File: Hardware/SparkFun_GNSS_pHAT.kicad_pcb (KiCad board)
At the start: 4 copper layers, 65 x 56.8 mm, 116 parts, among them J1 Raspberry_Pi_2x20_SMD_Passthr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, J2 Conn_02x10, J3 U.FL, J4 Conn_02x10, J5 microSD_Friction, J6 USB_C_Receptacle, J7 SMA_Edge, J8 Qwiic_Vertical, U1 CAT24C512WI-GT3, U2 AP7361C-3.3V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

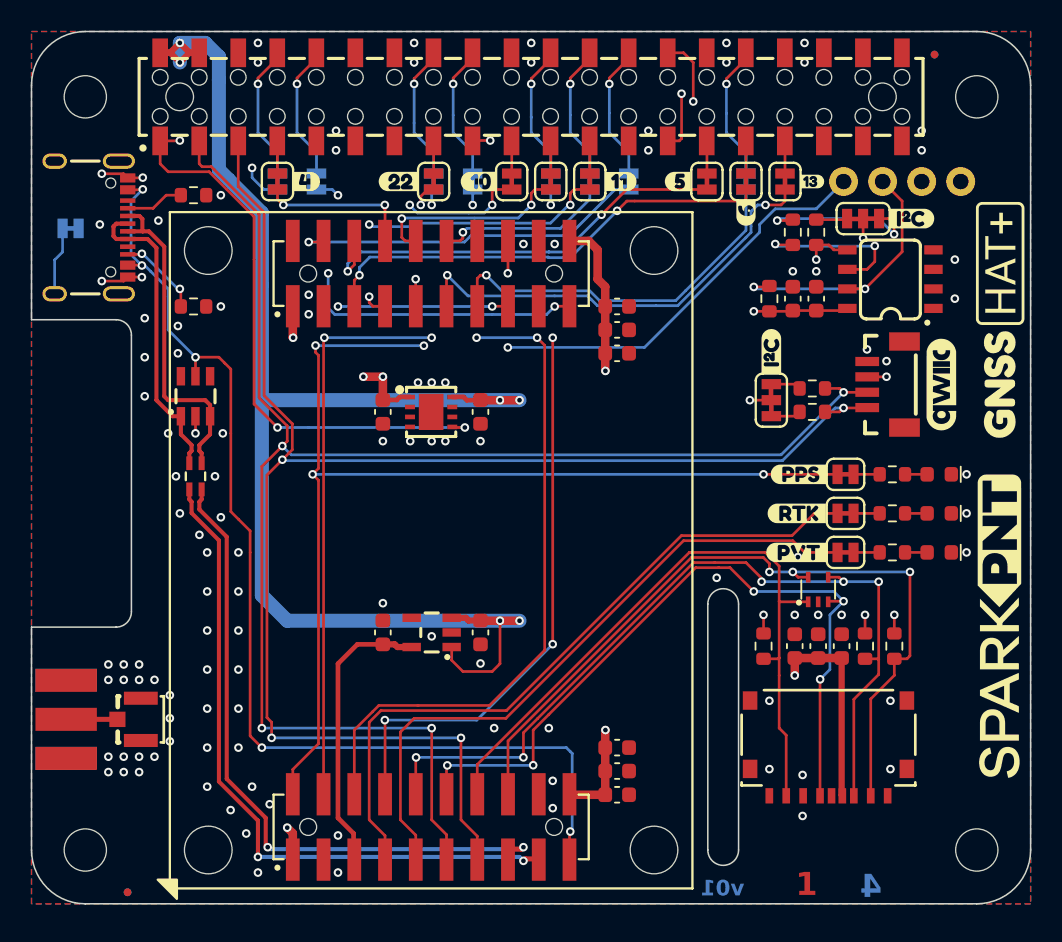
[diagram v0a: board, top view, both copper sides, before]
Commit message: pHAT routed and panelized
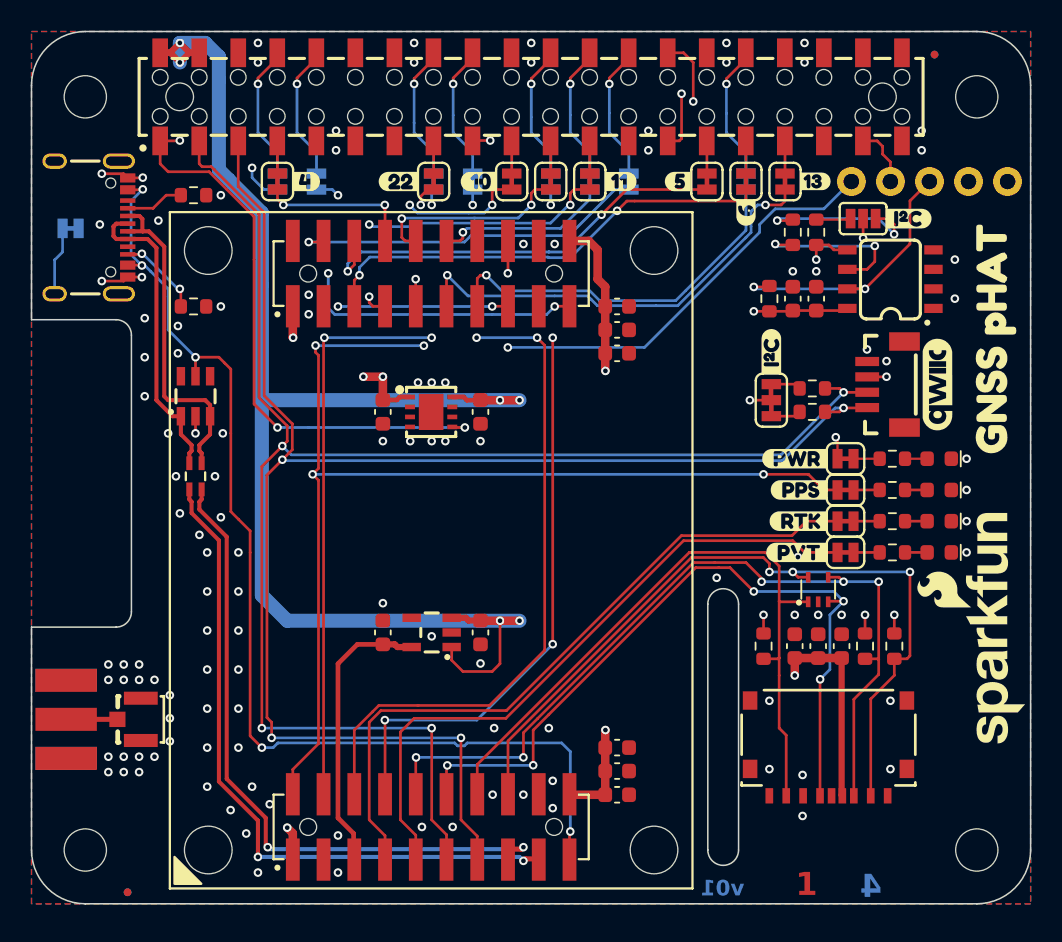
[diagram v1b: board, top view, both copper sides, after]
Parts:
- removed 3V3.1, GND.1, RST.1, WP.1: PTH, SparkFun-Connector:1x01
- removed the G*** at (178.6, 106.3)
- removed the G*** at (148.1, 97.0)
- removed REF** (x2): RPi_HAT+_8mm, SparkFun-Aesthetic:RPi_HAT+_8mm
- removed kibuzzard-678F852F (x2): G***, kibuzzard-678F852F
- removed kibuzzard-678F89CB: G***, kibuzzard-678F89CB
- removed kibuzzard-678F89E9: G***, kibuzzard-678F89E9
- removed kibuzzard-678F8DFF: G***, kibuzzard-678F8DFF
- removed kibuzzard-678F8FC6: G***, kibuzzard-678F8FC6
- added D6: Red, SparkFun-LED:LED_0603_1608Metric_Red, F.Cu at (174.6, 95.5)
- added G***: LOGO, SparkFun-Aesthetic:SparkFun_Logo_15mm, F.Cu at (178.1, 106.7)
- added G***: LOGO, SparkFun-Aesthetic:SparkFun_Logo_25mm, B.Cu at (148.3, 96.8)
- added J9: Conn_01x05, SparkFun-Connector:1x05, F.Cu at (179.1, 77.5)
- added JP23: ~, SparkFun-Jumper:Jumper_2_NC_Trace, F.Cu at (168.5, 95.5)
- added R14: 1k, SparkFun-Resistor:R_0603_1608Metric, F.Cu at (171.6, 95.5)
- added kibuzzard-67922B7F: G***, kibuzzard-67922B7F, F.Cu at (178.3, 87.7)
- added kibuzzard-67922E39: G***, kibuzzard-67922E39, F.Cu at (166.6, 77.5)
- added kibuzzard-67922EA6: G***, kibuzzard-67922EA6, B.Cu at (171.5, 79.6)
- added kibuzzard-67922FE7: G***, kibuzzard-67922FE7, F.Cu at (165.2, 95.5)
- added kibuzzard-67923645: G***, kibuzzard-67923645, B.Cu at (151.9, 79.6)
- added kibuzzard-679237A8: G***, kibuzzard-679237A8, B.Cu at (179.1, 80.0)
- added kibuzzard-679237B7: G***, kibuzzard-679237B7, B.Cu at (176.6, 79.8)
- added kibuzzard-67923C07: G***, kibuzzard-67923C07, B.Cu at (147.7, 102.4)
- D3: value Blue -> White; footprint SparkFun-LED:LED_0603_1608Metric_Blue -> SparkFun-LED:LED_0603_1608Metric_White
- D5: value Blue -> Yellow; footprint SparkFun-LED:LED_0603_1608Metric_Blue -> SparkFun-LED:LED_0603_1608Metric_Yellow
- JP2: footprint SparkFun-Jumper:Jumper_3_NC-2_Trace -> SparkFun-Jumper:Jumper_3_NO
- R11: value 2.2k -> 1k
- moved kibuzzard-678F918F 3.03 mm to (174.0, 79.9)
- moved D5 1.02 mm to (174.6, 97.5)
- moved JP22 1.02 mm to (168.5, 97.5)
- moved R13 1.02 mm to (171.6, 97.5)
- moved kibuzzard-678F8755 1.02 mm to (165.5, 97.5)
- moved kibuzzard-678F8777 0.52 mm to (165.5, 99.6)
- moved D3 0.51 mm to (174.6, 99.6)
- moved JP20 0.51 mm to (168.5, 99.6)
- moved R11 0.51 mm to (171.6, 99.6)
- moved kibuzzard-678F8AD2 0.47 mm to (168.9, 80.0)
- moved G*** 0.25 mm to (174.5, 90.7)
- moved kibuzzard-678F893B 0.18 mm to (172.7, 79.9)
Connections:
- net Net-(U1-WP) renamed WP
- J1 pad 37: unconnected-(J1-GPIO26-Pad37) -> GPIO26
- J4 pad 16: Net-(J4-Pin_2-Pad16) -> ~{RST}
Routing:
- net ~{RST}: track 0.00 -> 34.1 mm, vias 0 -> 2
- net Net-(J4-Pin_2-Pad16): track 33.5 -> 0.00 mm, vias 2 -> 0
- net GPIO26: track 0.00 -> 3.93 mm
- net Net-(JP23-A): track 0.00 -> 1.70 mm
- net 3.3V: track 53.8 -> 55.2 mm, vias 14 -> 15
- net Net-(D6-A): track 0.00 -> 1.44 mm
- net GND: vias 113 -> 118
